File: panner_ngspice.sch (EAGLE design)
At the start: 49 parts, among them U1 MAX5419LETA+, U2 MAX5419LETA+, X1 OPAMP, X10 OPAMP, X3 OPAMP, X5 OPAMP, X6 OPAMP, X7 OPAMP, X8 OPAMP, X9 OPAMP

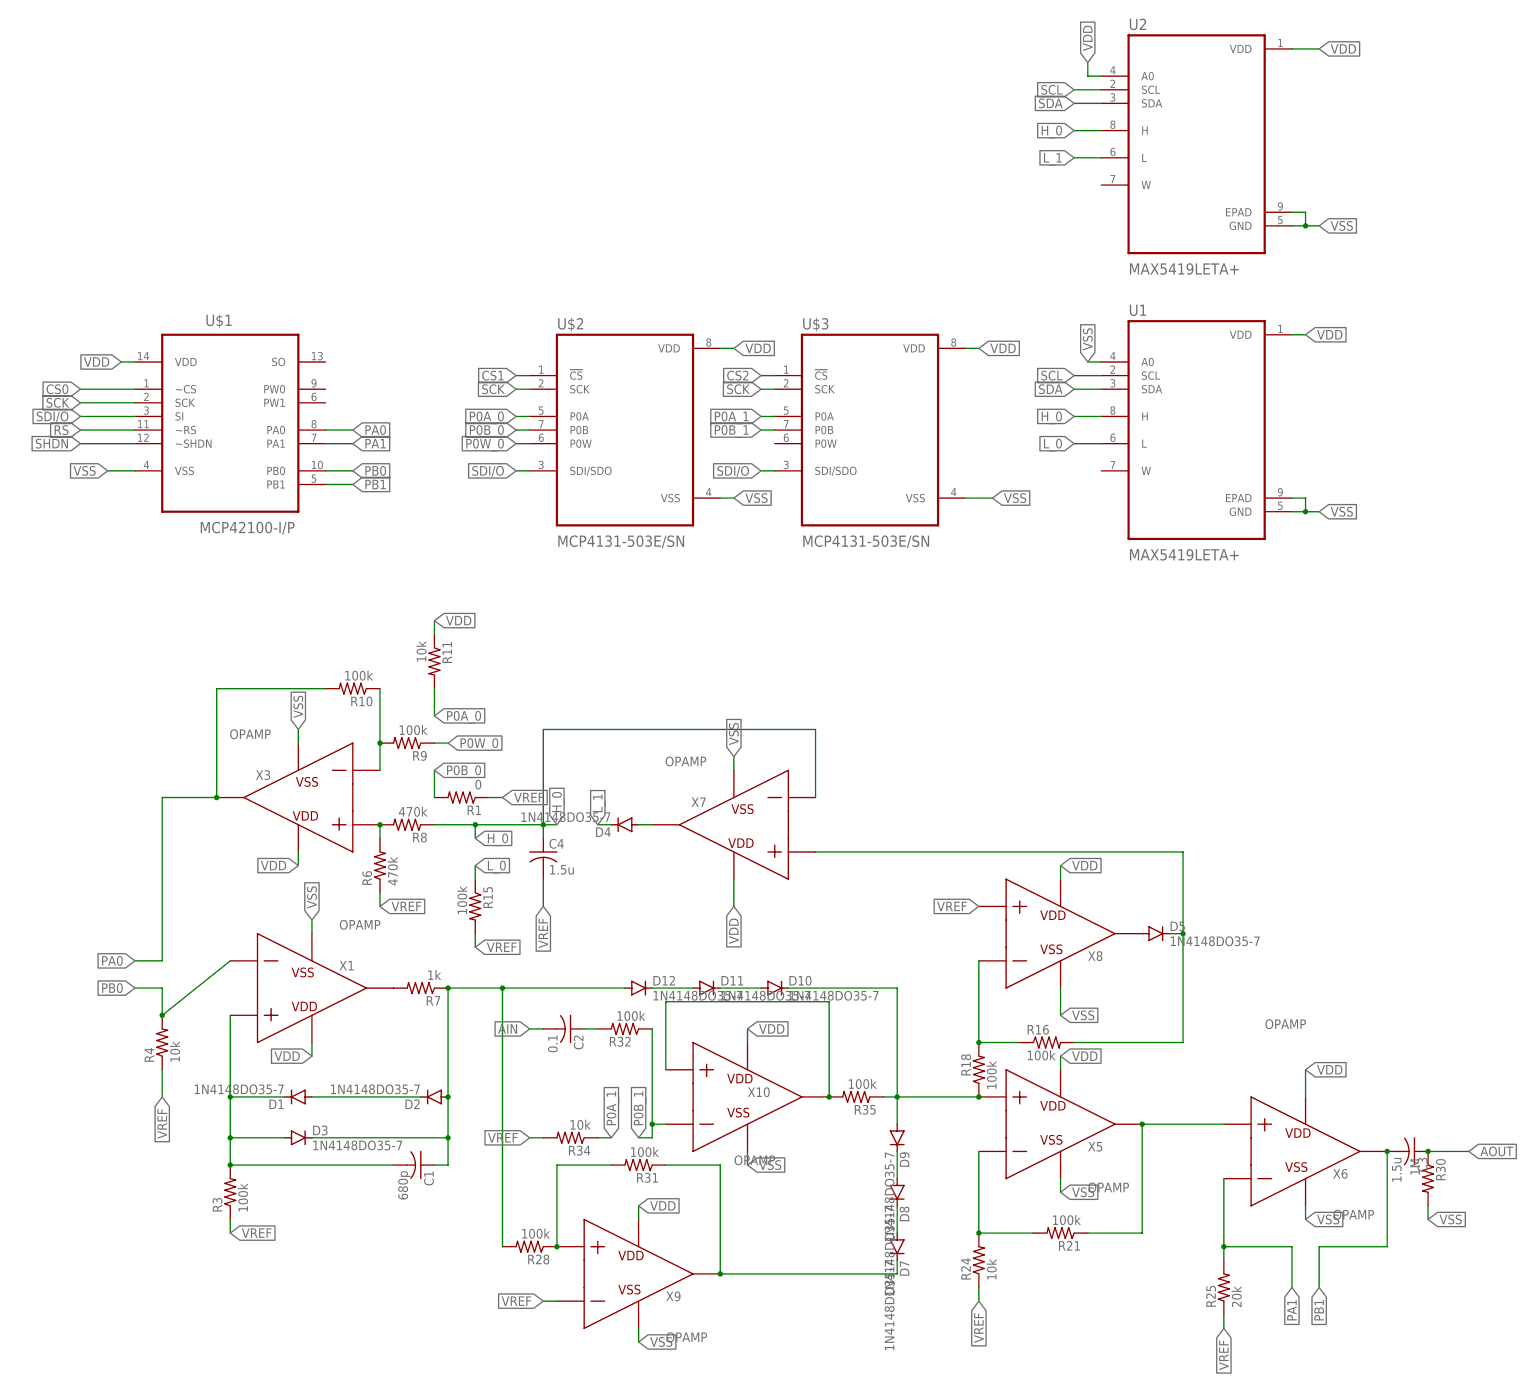
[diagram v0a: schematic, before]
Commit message: update, split out into schematics for each component
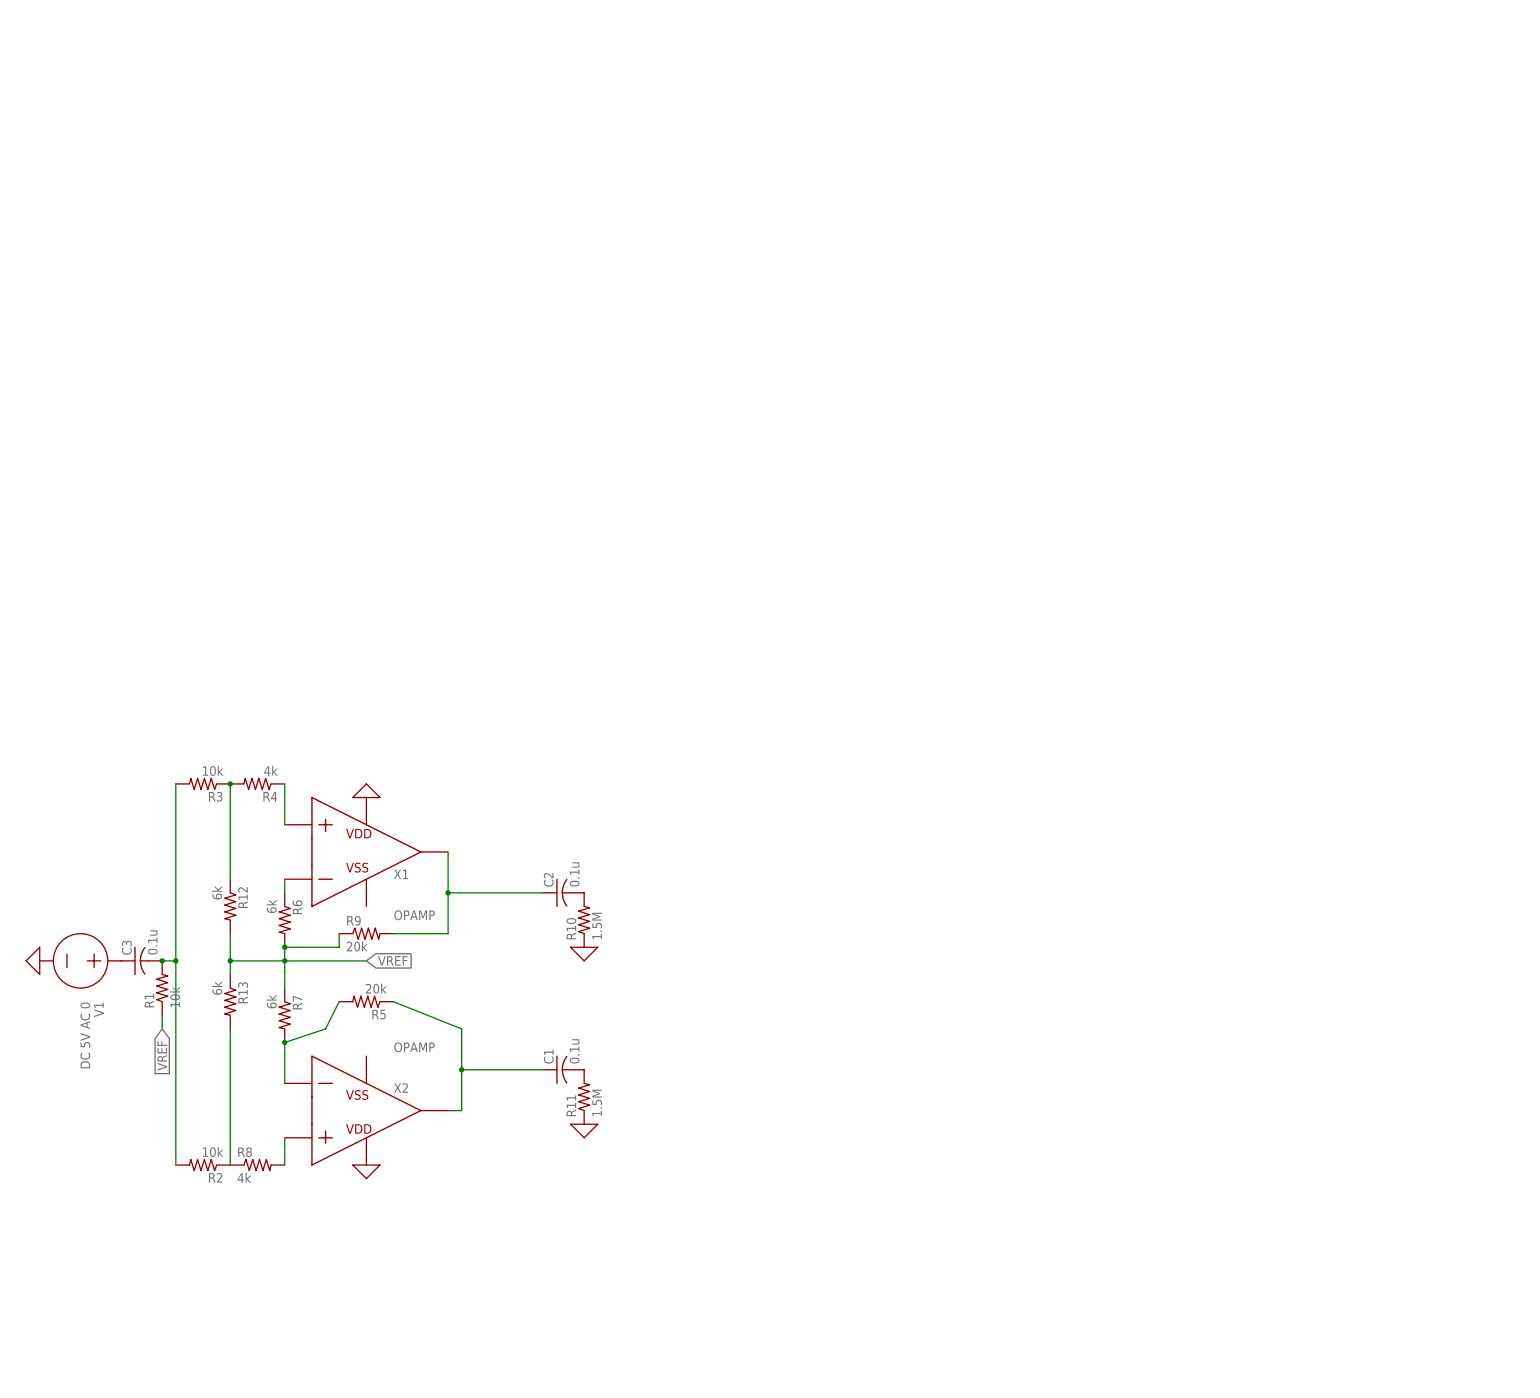
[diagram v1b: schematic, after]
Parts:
- removed C4: 1.5u, rcl:C-US025-024X044
- removed D1, D10, D11, D12, D2, D3, D4, D5, D7, D8, D9: 1N4148DO35-7, diode:1N4148DO35-7
- removed R15, R16, R18, R21, R28, R31, R32, R35: 100k, rcl:R-US_0204/7
- removed R24, R34: 10k, rcl:R-US_0204/7
- removed R25: 20k, rcl:R-US_0204/7
- removed R30: 1M, rcl:R-US_0204/7
- removed U$1: MCP42100-I/P, MCP42100-I_P:MCP42100-I/P
- removed U$2, U$3: MCP4131-503E/SN, MCP4131-503E_SN:MCP4131-503E/SN
- removed U1, U2: MAX5419LETA+, MAX5419LETA_:MAX5419LETA+
- removed X10, X3, X5, X6, X7, X8, X9: OPAMP, ngspice-simulation:OPAMP
- added R12, R13: 6k, rcl:R-US_0204/5
- added R2: 10k, rcl:R-US_0204/5
- added R5: 20k, rcl:R-US_0204/5
- added V1: DC 5V AC 0, ngspice-simulation:VOLTAGE
- added X2: OPAMP, ngspice-simulation:OPAMP
- C1: value 680p -> 0.1u
- C2: value 0.1 -> 0.1u
- C3: value 1.5u -> 0.1u
- R1: value 0 -> 10k; device rcl:R-US_0204/7 -> rcl:R-US_0204/5
- R10: value 100k -> 1.5M; device rcl:R-US_0204/7 -> rcl:R-US_0204/5
- R11: value 10k -> 1.5M; device rcl:R-US_0204/7 -> rcl:R-US_0204/5
- R3: value 100k -> 10k; device rcl:R-US_0204/7 -> rcl:R-US_0204/5
- R4: value 10k -> 4k; device rcl:R-US_0204/7 -> rcl:R-US_0204/5
- R6: value 470k -> 6k; device rcl:R-US_0204/7 -> rcl:R-US_0204/5
- R7: value 1k -> 6k; device rcl:R-US_0204/7 -> rcl:R-US_0204/5
- R8: value 470k -> 4k; device rcl:R-US_0204/7 -> rcl:R-US_0204/5
- R9: value 100k -> 20k; device rcl:R-US_0204/7 -> rcl:R-US_0204/5
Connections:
- removed net AIN: C2.2
- removed net AOUT: C3.1, R30.1
- removed net CS0: U$1.~CS
- removed net CS1: U$2.!CS
- removed net CS2: U$3.!CS
- removed net H_0: C4.1, R8.1, U1.H, U2.H, X7.N
- removed net L_0: R15.1, U1.L
- removed net L_1: D4.C, U2.L
- removed net N$14: D4.A, X7.VOUT
- removed net N$15: D5.C, R16.2, X7.P
- removed net N$16: R16.1, R18.2, X8.N
- removed net N$18: R21.1, X5.VOUT, X6.P
- removed net N$19: R21.2, R24.2, X5.N
- removed net N$20: D1.A, D2.C
- removed net N$21: C1.1, D12.A, D2.A, D3.C, R28.2, R7.1
- removed net N$22: R28.1, R31.2, X9.P
- removed net N$23: D7.C, R31.1, X9.VOUT
- removed net N$24: D8.A, D9.C
- removed net N$25: D7.A, D8.C
- removed net N$26: D10.C, D9.A, R18.1, R35.1, X5.P
- removed net N$27: R35.2, X10.P, X10.VOUT
- removed net N$3: C1.2, D1.C, D3.A, R3.2, X1.P
- removed net N$30: C2.1, R32.2
- removed net N$31: D11.A, D12.C
- removed net N$32: D10.A, D11.C
- removed net N$33: D5.A, X8.VOUT
- removed net P0A_0: R11.2, U$2.P0A
- removed net P0A_1: R34.1, U$3.P0A
- removed net P0B_0: R1.2, U$2.P0B
- removed net P0B_1: R32.1, U$3.P0B, X10.N
- removed net P0W_0: R9.1, U$2.P0W
- removed net PA0: R10.2, U$1.PA0, X3.VOUT
- removed net PA1: R25.2, U$1.PA1, X6.N
- removed net PB0: R4.2, U$1.PB0, X1.N
- removed net PB1: C3.2, U$1.PB1, X6.VOUT
- removed net RS: U$1.~RS
- removed net SCK: U$1.SCK, U$2.SCK, U$3.SCK
- removed net SCL: U1.SCL, U2.SCL
- removed net SDA: U1.SDA, U2.SDA
- removed net SDI/O: U$1.SI, U$2.SDI/SDO, U$3.SDI/SDO
- removed net SHDN: U$1.~SHDN
- removed net VDD: R11.1, U$1.VDD, U$2.VDD, U$3.VDD, U1.VDD, U2.A0, U2.VDD, X1.VDD, X10.VDD, X3.VDD, X5.VDD, X6.VDD, X7.VDD, X8.VDD, X9.VDD
- removed net VSS: R30.2, U$1.VSS, U$2.VSS, U$3.VSS, U1.A0, U1.EPAD, U1.GND, U2.EPAD, U2.GND, X1.VSS, X10.VSS, X3.VSS, X5.VSS, X6.VSS, X7.VSS, X8.VSS, X9.VSS
- new net 0: R10.1, R11.1, V1.-, X1.VDD, X2.VDD
- new net N$10: C1.2, R11.2
- new net N$11: C2.2, R10.2
- new net N$12: R8.2, X2.P
- new net N$13: R4.1, X1.P
- new net N$2: C3.2, R1.2, R2.2, R3.2
- new net N$4: R2.1, R8.1
- new net N$8: C1.1, R5.1, X2.VOUT
- new net N$9: C2.1, R9.2, X1.VOUT
- new net P0A: R12.1, R3.1, R4.2
- new net P0B: R13.2
- net N$1: now also C3.1, V1.+; no longer R7.2, X1.VOUT
- net N$6: now also R6.1, X1.N; no longer R6.2, R8.2, X3.P
- net N$7: now also R5.2, R7.2, X2.N; no longer R10.1, R9.2, X3.N
- net VREF: now also R12.2, R13.1, R6.2, R7.1, R9.1; no longer C4.2, R15.2, R24.1, R25.1, R3.1, R34.2, R4.1, R6.1, X9.N
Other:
- moved on the sheet: C1, C2, C3, R1, R10, R11, R3, R4, R6, R7, R8, R9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
